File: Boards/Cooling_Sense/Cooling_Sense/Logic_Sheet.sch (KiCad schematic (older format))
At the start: 45 parts

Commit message: updated schematic with new analog circuitry, waiting for ok from manu to proceed
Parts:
- removed D? (x5): LED_0805, footprints:LED_0805_OEM, symbol formula:LED_0805
- removed R? (x25): R, symbol Device:R
- removed U? (x10): MCP6001T-I-LT, Package_TO_SOT_SMD:SOT-353_SC-70-5, symbol formula:MCP6001T-I-LT
- removed U? (x5): 74LVC2G02, symbol 74xGxx:74LVC2G02
- added R?: R_1K, footprints:R_0805_OEM, symbol formula:R_1K
- added R? (x4): R_3K, footprints:R_0805_OEM, symbol formula:R_3K
- added R?: R_10K, footprints:R_0805_OEM, symbol formula:R_10K
- added R?: R_22K, footprints:R_0805_OEM, symbol formula:R_22K
- added U? (x2): MCP6001T-I-LT, Package_TO_SOT_SMD:SOT-353_SC-70-5, symbol formula:MCP6001T-I-LT
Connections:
- net labels added: SENSE_1+, SENSE_1-, SENSE_1_OUT
- net labels removed: CONTROLLER_PRESSURE_SENSE_CHECK, CONTROLLER_TEMP_SENSE_CHECK, MOTOR_TEMP_SENSE_CHECK, PUMP_PRESSURE_SENSE_CHECK, RADIATOR_TEMP_SENSE_CHECK
- wire segments 60 -> 20
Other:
- note removed: "If LED is on, sensor is good"

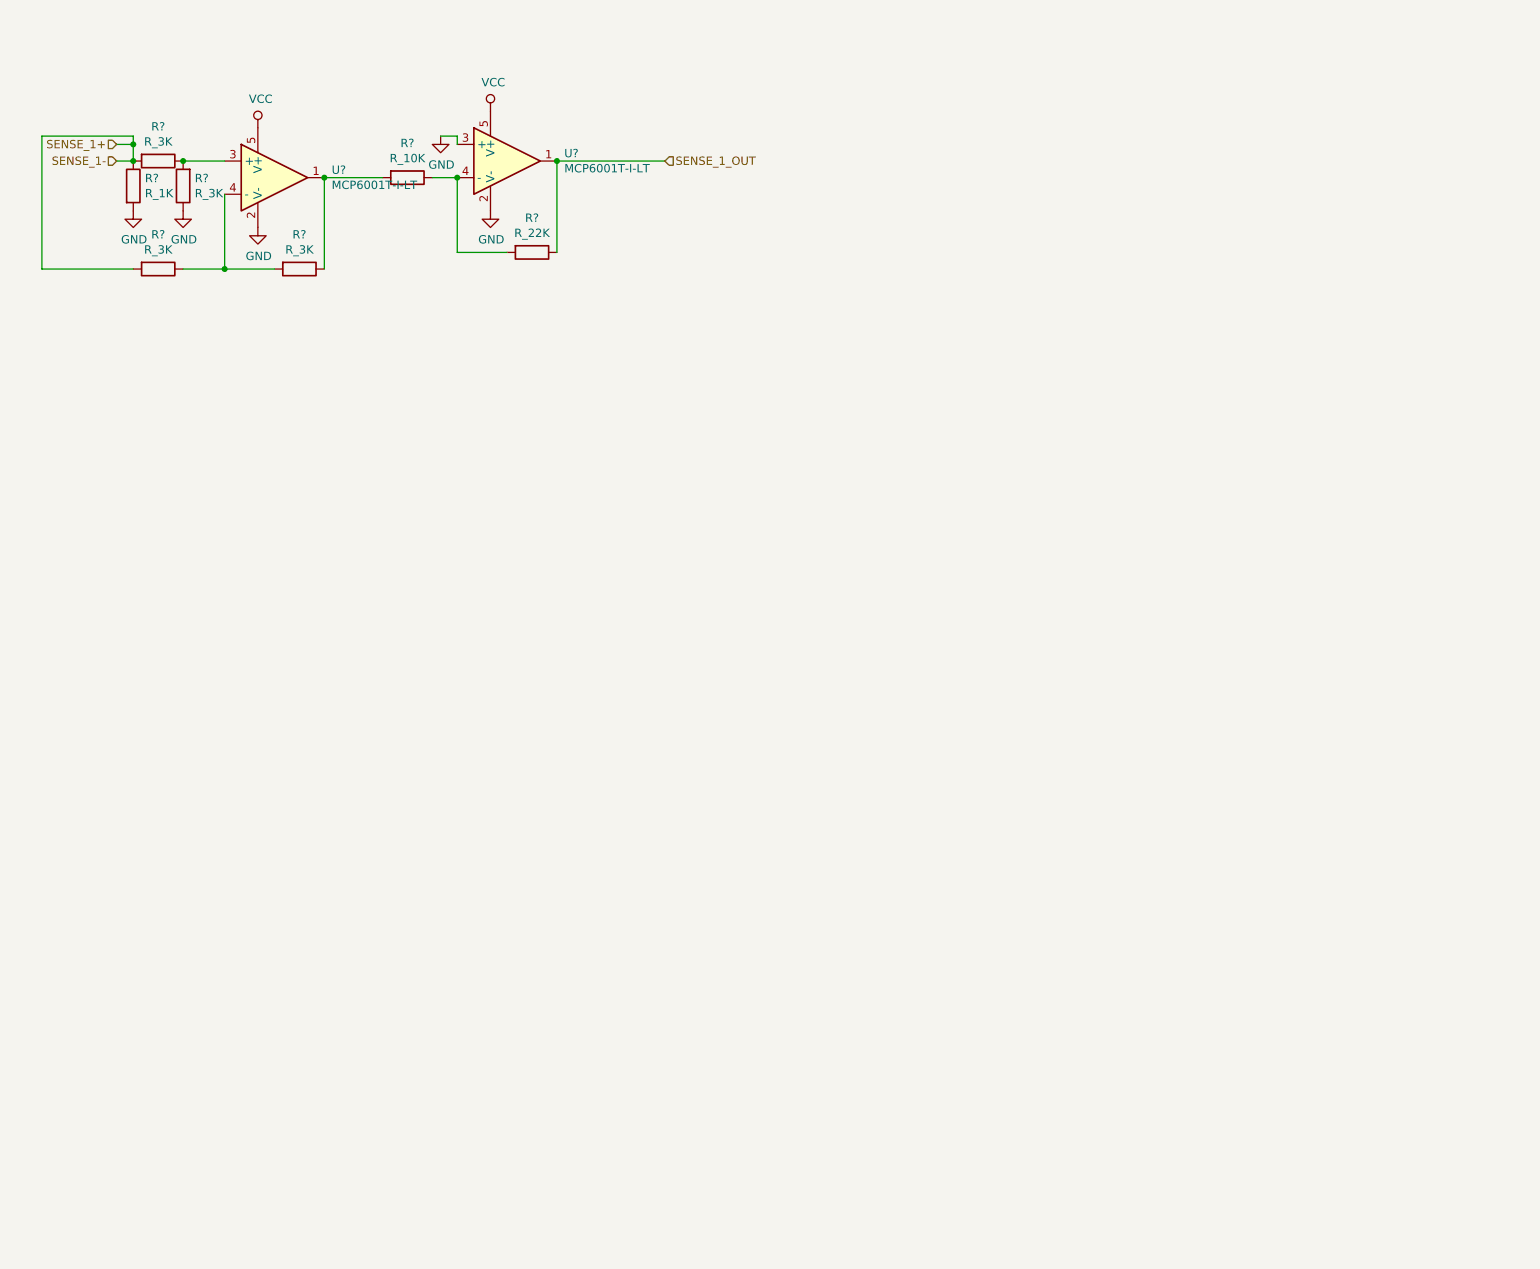
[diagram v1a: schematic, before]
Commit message: minor schematic fixes, began layout
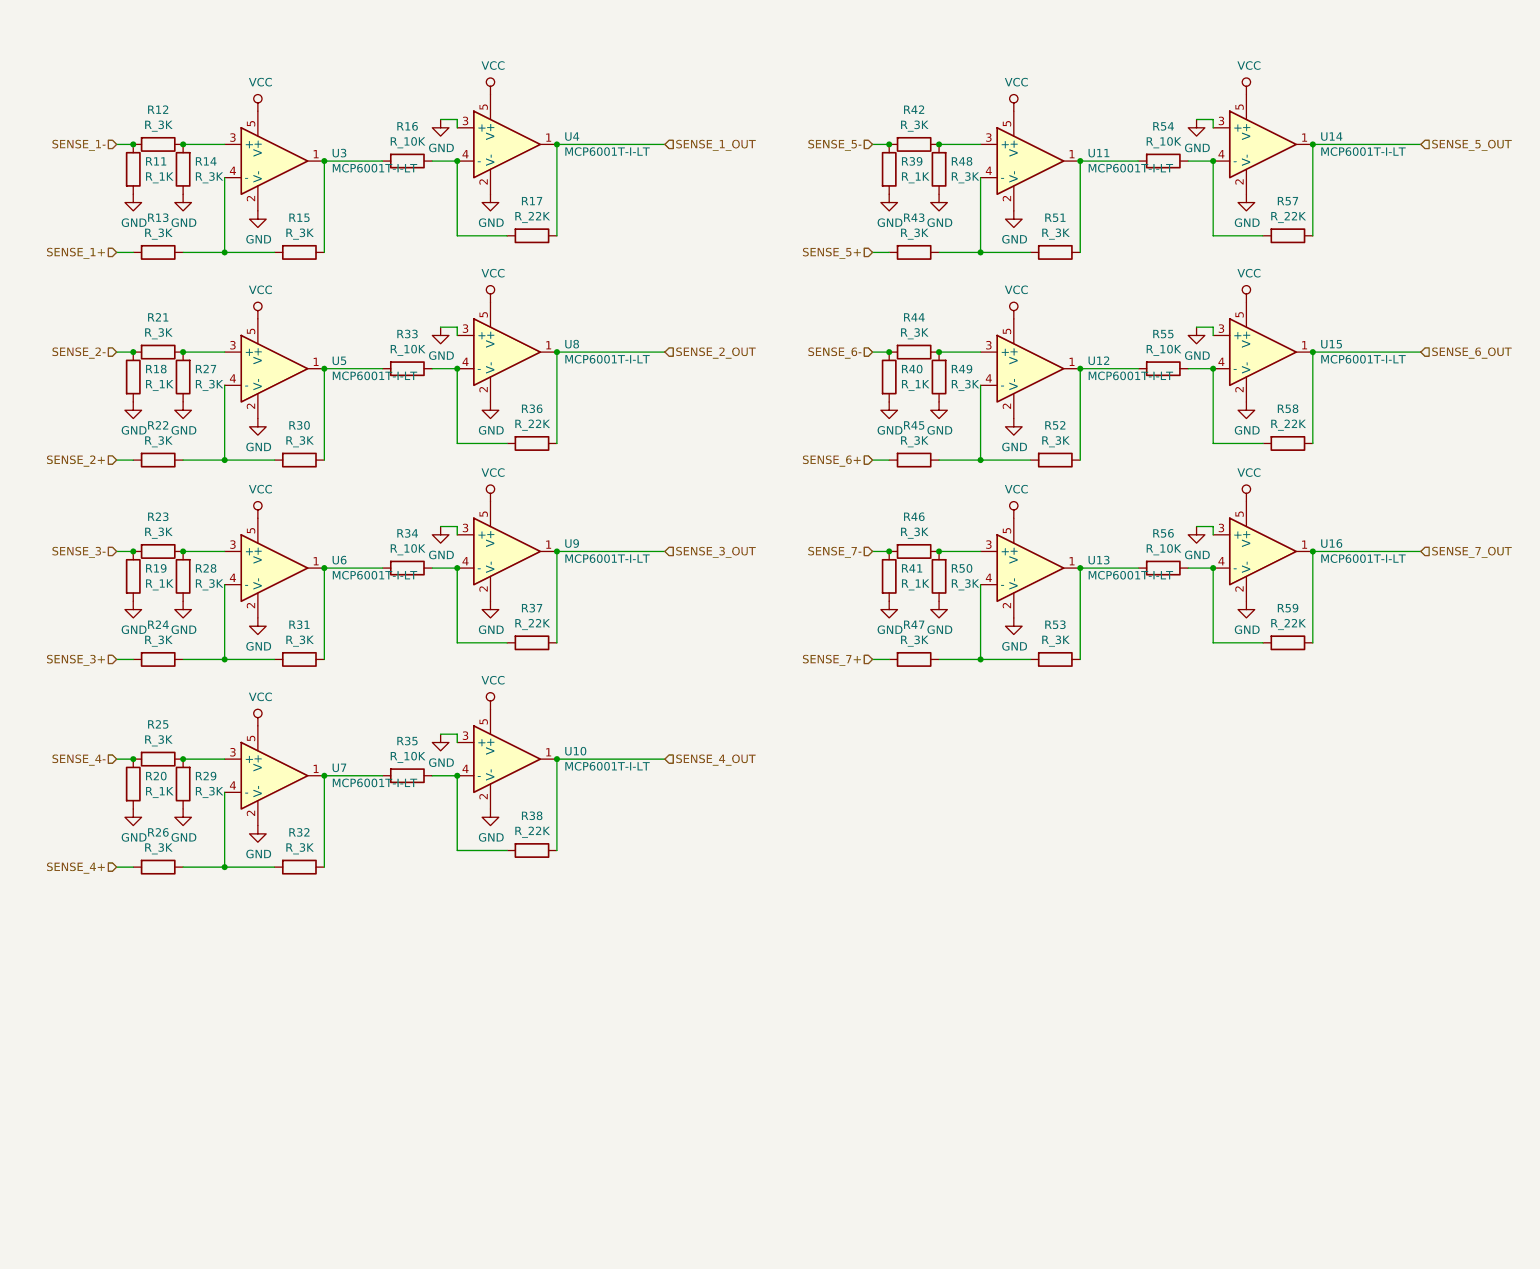
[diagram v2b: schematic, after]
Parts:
- added R18, R19, R20, R39, R40, R41: R_1K, footprints:R_0805_OEM, symbol formula:R_1K
- added R21, R22, R23, R24, R25, R26, R27, R28, R29, R30, R31, R32, R42, R43, R44, R45, R46, R47, R48, R49, R50, R51, R52, R53: R_3K, footprints:R_0805_OEM, symbol formula:R_3K
- added R33, R34, R35, R54, R55, R56: R_10K, footprints:R_0805_OEM, symbol formula:R_10K
- added R36, R37, R38, R57, R58, R59: R_22K, footprints:R_0805_OEM, symbol formula:R_22K
- added U10, U11, U12, U13, U14, U15, U16, U5, U6, U7, U8, U9: MCP6001T-I-LT, Package_TO_SOT_SMD:SOT-353_SC-70-5, symbol formula:MCP6001T-I-LT
- gave numbers to parts that had none: 9
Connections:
- net GND: now also R18.2, R19.2, R20.2, R27.1, R28.1, R29.1, R39.2, R40.2, R41.2, R48.1, R49.1, R50.1, U10.2 (V-), U10.3 (+), U11.2 (V-), U12.2 (V-), U13.2 (V-), U14.2 (V-), U14.3 (+), U15.2 (V-), U15.3 (+), U16.2 (V-), U16.3 (+), U5.2 (V-), U6.2 (V-), U7.2 (V-), U8.2 (V-), U8.3 (+), U9.2 (V-), U9.3 (+)
- net SENSE_1+: no longer R11.1, R12.2
- net VCC: now also U10.5 (V+), U11.5 (V+), U12.5 (V+), U13.5 (V+), U14.5 (V+), U15.5 (V+), U16.5 (V+), U5.5 (V+), U6.5 (V+), U7.5 (V+), U8.5 (V+), U9.5 (V+)
- new net: R21.1, R27.2, U5.3 (+)
- new net: R22.1, R30.2, U5.4 (-)
- new net: R30.1, R33.2, U5.1
- new net: R33.1, R36.2, U8.4 (-)
- new net: R23.1, R28.2, U6.3 (+)
- new net: R24.1, R31.2, U6.4 (-)
- new net: R31.1, R34.2, U6.1
- new net: R34.1, R37.2, U9.4 (-)
- new net: R25.1, R29.2, U7.3 (+)
- new net: R26.1, R32.2, U7.4 (-)
- new net: R32.1, R35.2, U7.1
- new net: R35.1, R38.2, U10.4 (-)
- new net: R42.1, R48.2, U11.3 (+)
- new net: R43.1, R51.2, U11.4 (-)
- new net: R51.1, R54.2, U11.1
- new net: R54.1, R57.2, U14.4 (-)
- new net: R44.1, R49.2, U12.3 (+)
- new net: R45.1, R52.2, U12.4 (-)
- new net: R52.1, R55.2, U12.1
- new net: R55.1, R58.2, U15.4 (-)
- new net: R46.1, R50.2, U13.3 (+)
- new net: R47.1, R53.2, U13.4 (-)
- new net: R53.1, R56.2, U13.1
- new net: R56.1, R59.2, U16.4 (-)
- new net SENSE_1-: R11.1, R12.2
- new net SENSE_2+: R22.2
- new net SENSE_2-: R18.1, R21.2
- new net SENSE_2_OUT: R36.1, U8.1
- new net SENSE_3+: R24.2
- new net SENSE_3-: R19.1, R23.2
- new net SENSE_3_OUT: R37.1, U9.1
- new net SENSE_4+: R26.2
- new net SENSE_4-: R20.1, R25.2
- new net SENSE_4_OUT: R38.1, U10.1
- new net SENSE_5+: R43.2
- new net SENSE_5-: R39.1, R42.2
- new net SENSE_5_OUT: R57.1, U14.1
- new net SENSE_6+: R45.2
- new net SENSE_6-: R40.1, R44.2
- new net SENSE_6_OUT: R58.1, U15.1
- new net SENSE_7+: R47.2
- new net SENSE_7-: R41.1, R46.2
- new net SENSE_7_OUT: R59.1, U16.1
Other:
- moved on the sheet: R11, R12, R13, R14, R15, R16, R17, U3, U4

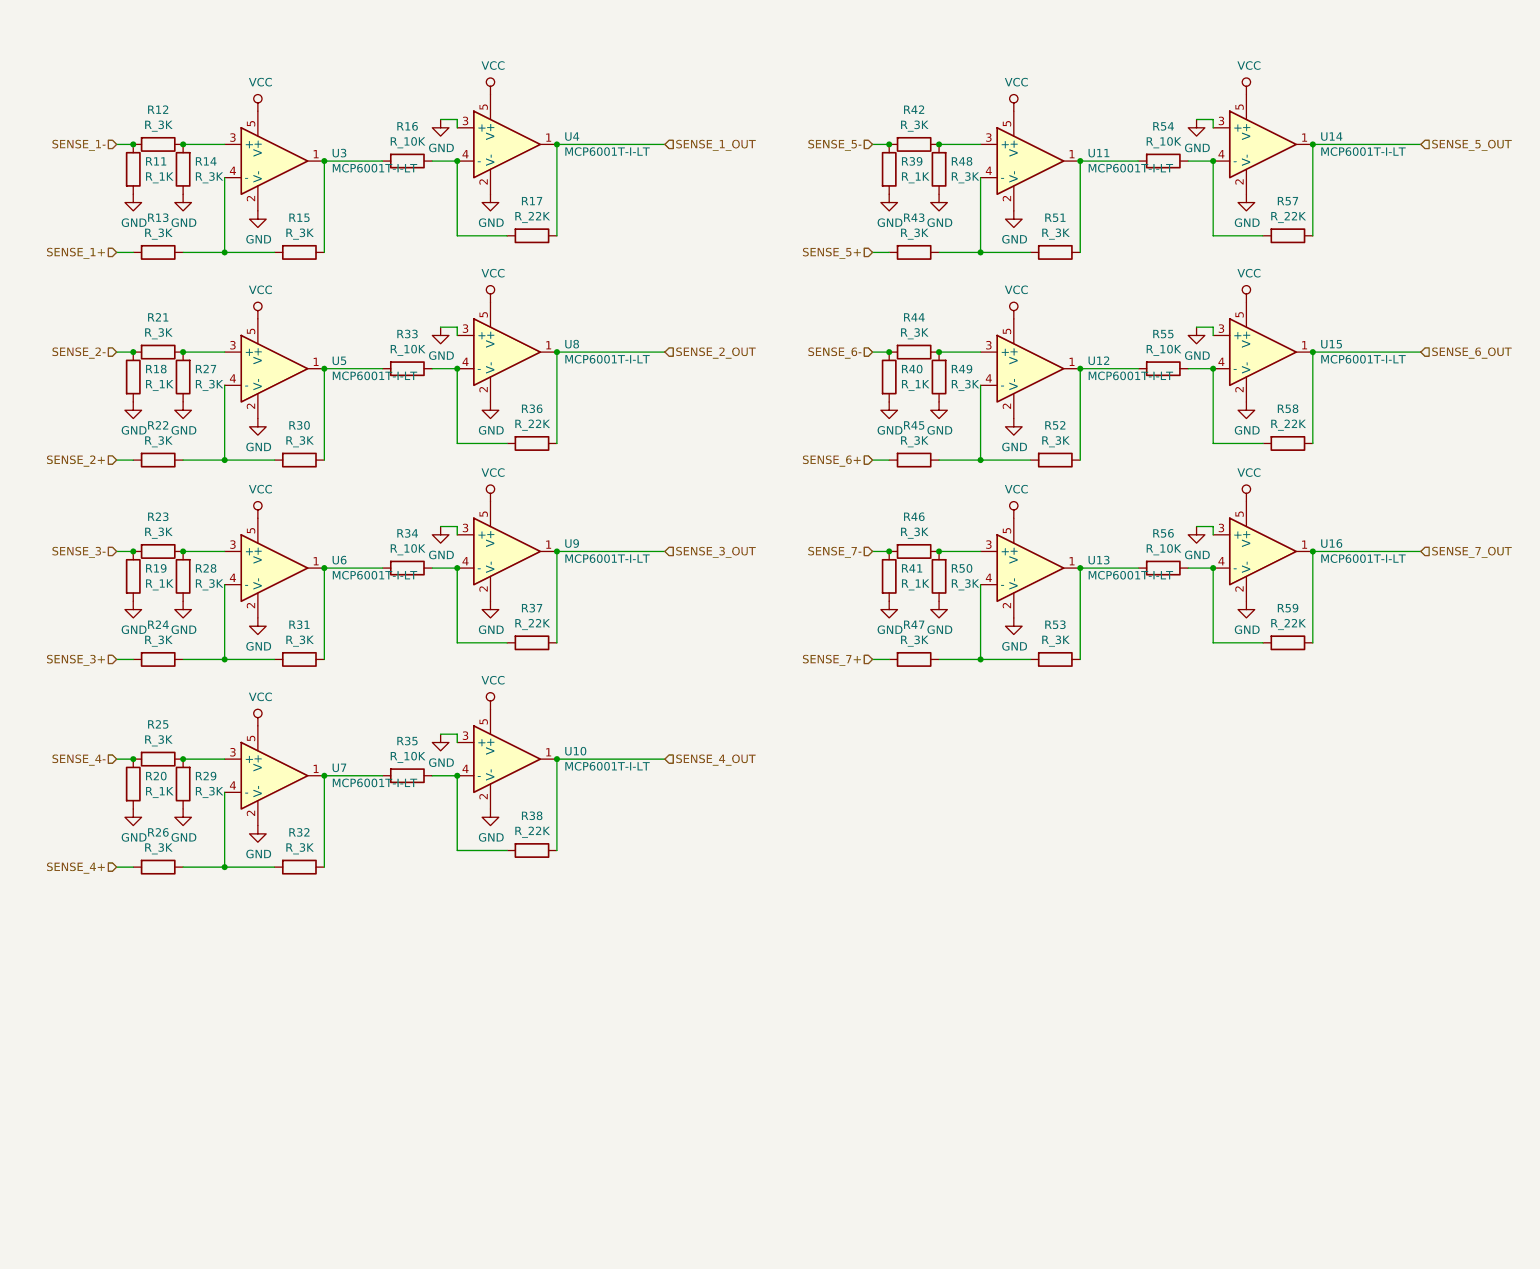
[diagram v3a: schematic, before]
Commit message: updated to new version of logic circuit
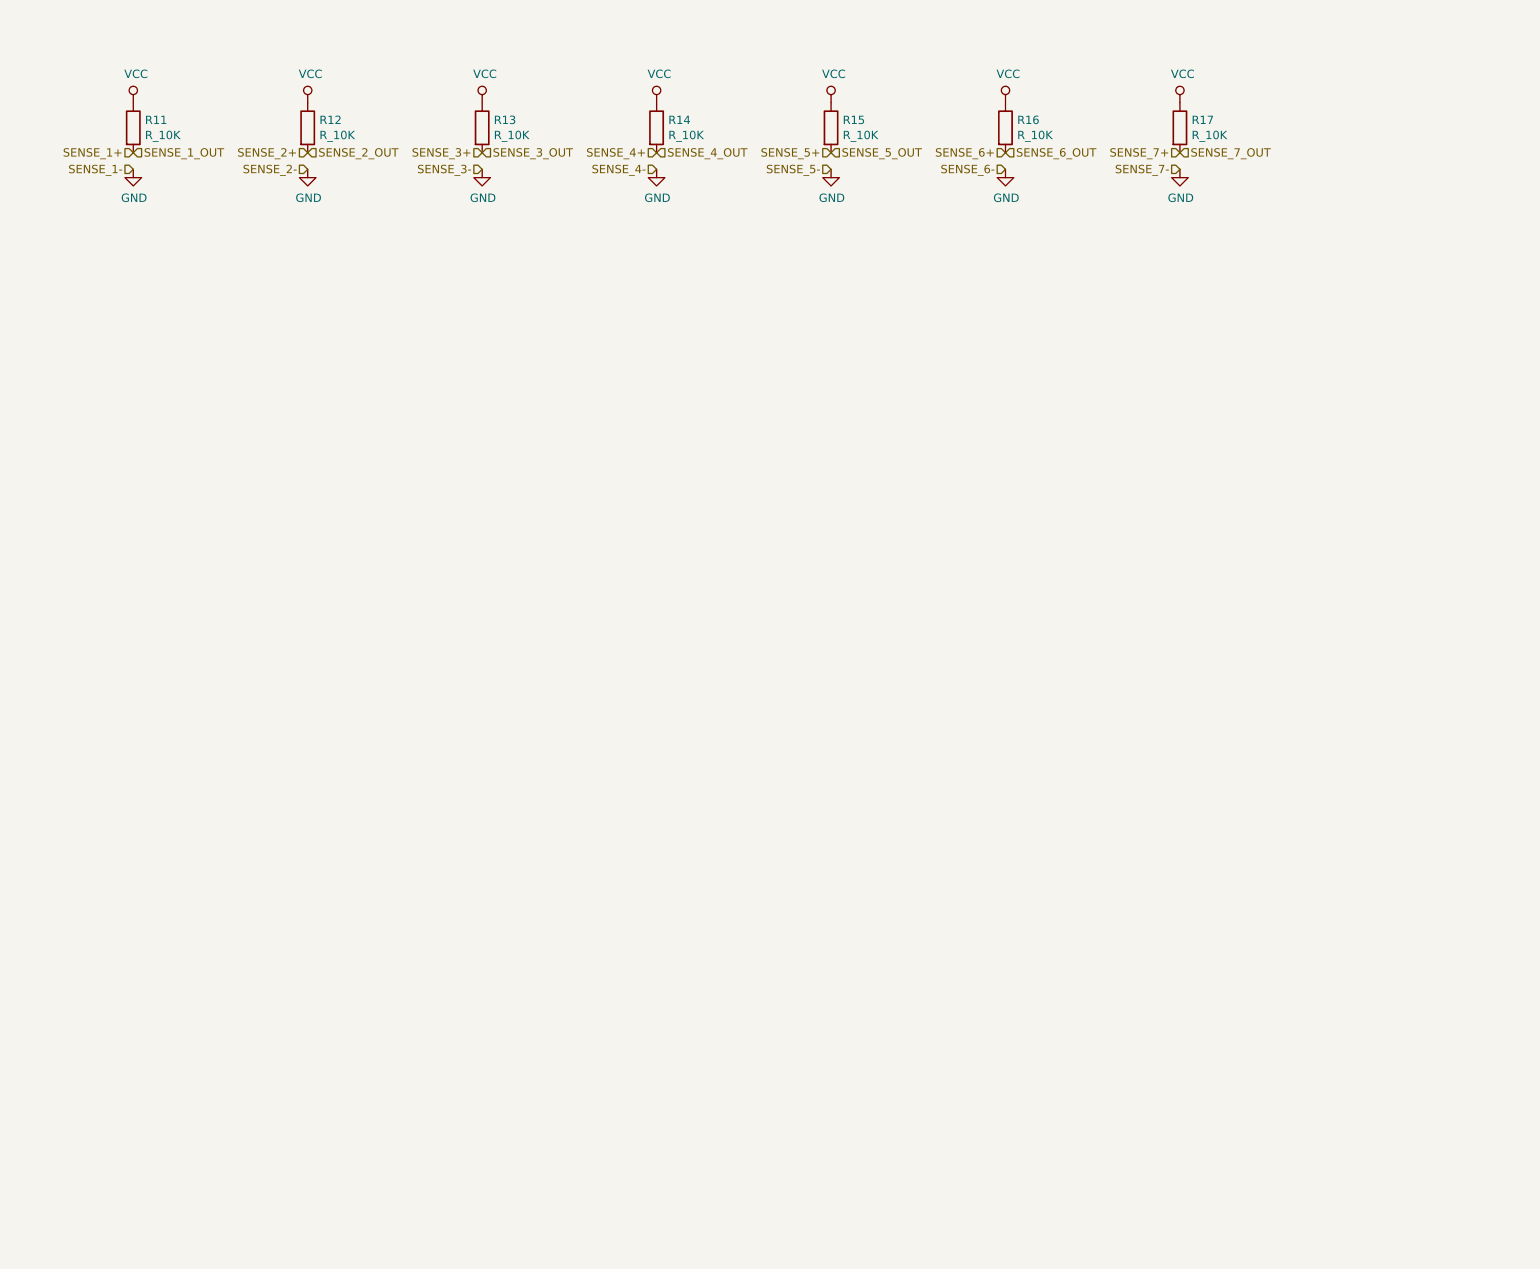
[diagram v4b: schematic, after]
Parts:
- removed R11, R18, R19, R20, R39, R40, R41: R_1K, footprints:R_0805_OEM, symbol formula:R_1K
- removed R12, R13, R14, R15, R21, R22, R23, R24, R25, R26, R27, R28, R29, R30, R31, R32, R42, R43, R44, R45, R46, R47, R48, R49, R50, R51, R52, R53: R_3K, footprints:R_0805_OEM, symbol formula:R_3K
- removed R17, R36, R37, R38, R57, R58, R59: R_22K, footprints:R_0805_OEM, symbol formula:R_22K
- removed R33, R34, R35, R54, R55, R56: R_10K, footprints:R_0805_OEM, symbol formula:R_10K
- removed U10, U11, U12, U13, U14, U15, U16, U3, U4, U5, U6, U7, U8, U9: MCP6001T-I-LT, Package_TO_SOT_SMD:SOT-353_SC-70-5, symbol formula:MCP6001T-I-LT
- added R11, R12, R13, R14, R15, R17: R_10K, footprints:R_0805_OEM, symbol formula:R_10K
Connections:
- net SENSE_1+: now also R11.2
- net SENSE_2+: now also R12.2
- net SENSE_3+: now also R13.2
- net SENSE_4+: now also R14.2
- net SENSE_5+: now also R15.2
- net SENSE_6+: now also R16.2
- net SENSE_7+: now also R17.2
- net VCC: now also R16.1, R11.1, R12.1, R13.1, R14.1, R15.1, R17.1
